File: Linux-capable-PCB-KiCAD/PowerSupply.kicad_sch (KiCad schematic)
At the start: 59 parts

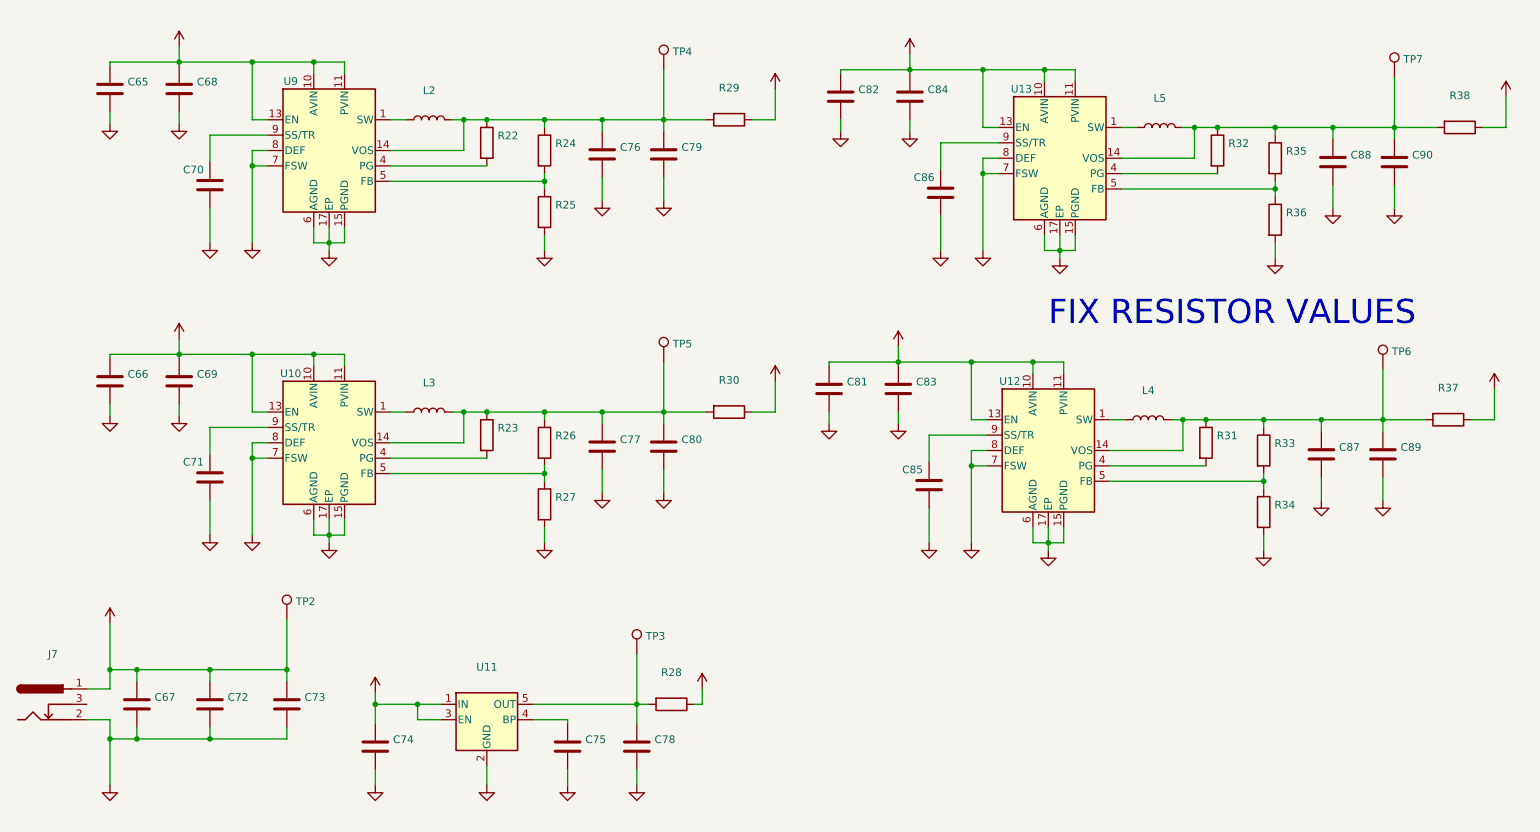
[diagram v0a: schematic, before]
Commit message: Dodao 3.3V na SD karticu, treba zamjeniti SD konektor, zavrsio napjanje, treba izracunati vrijednosti otpornika i footprint preci za komponente
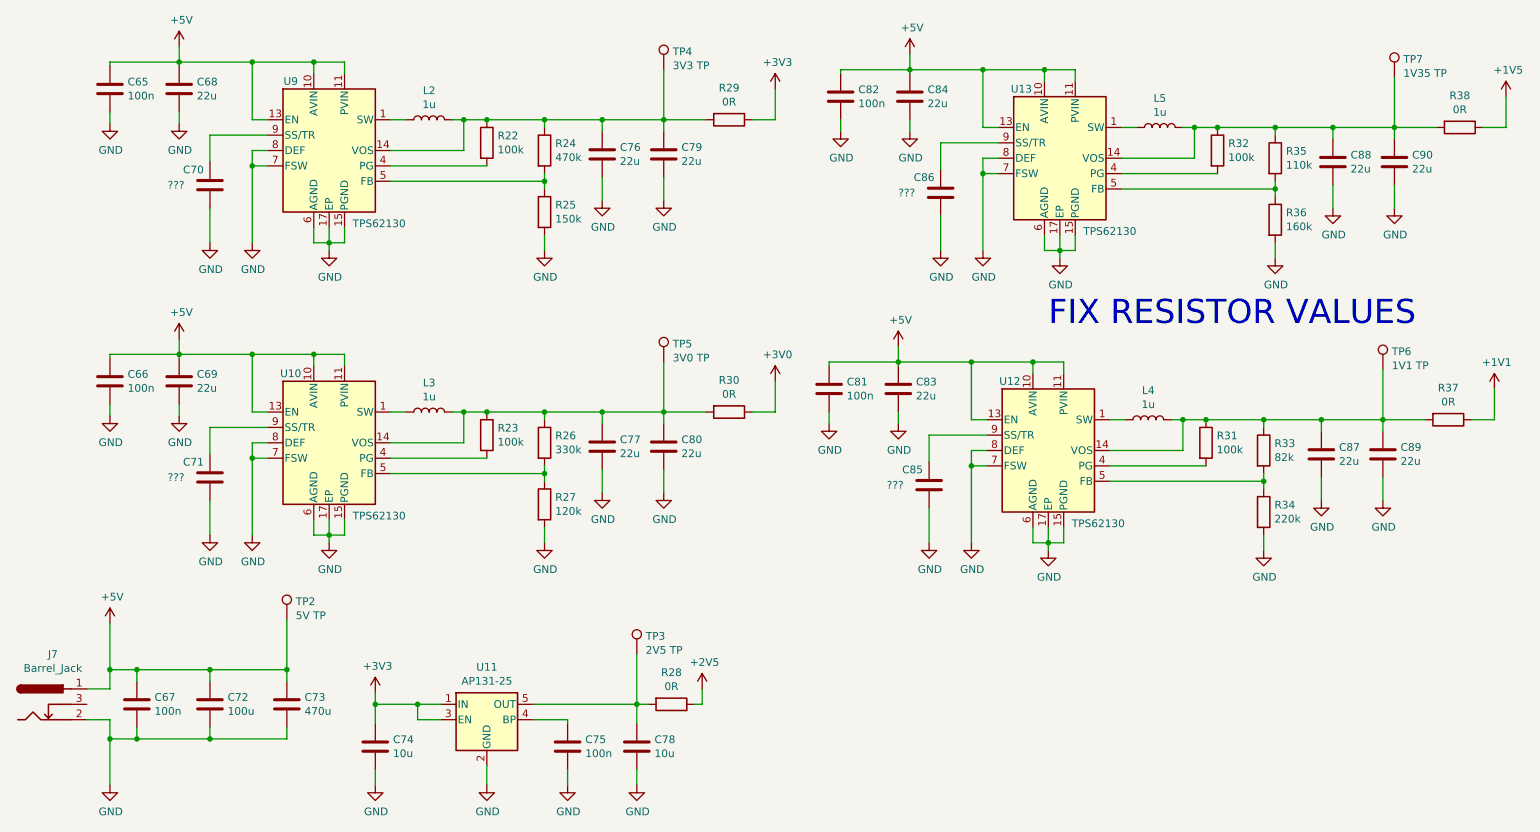
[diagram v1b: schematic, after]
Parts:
- C65, C66, C67, C75, C81, C82: value (none) -> 100n; footprint (none) -> Capacitor_SMD:C_0603_1608Metric
- C68, C69, C76, C77, C79, C80, C83, C84, C87, C88, C89, C90: value (none) -> 22u; footprint (none) -> Capacitor_SMD:C_0603_1608Metric
- C70, C71, C85, C86: value (none) -> ???; footprint (none) -> Capacitor_SMD:C_0603_1608Metric
- C72: value (none) -> 100u; footprint (none) -> Capacitor_SMD:C_0603_1608Metric
- C73: value (none) -> 470u; footprint (none) -> Capacitor_SMD:C_0603_1608Metric
- C74, C78: value (none) -> 10u; footprint (none) -> Capacitor_SMD:C_0603_1608Metric
- J7: value (none) -> Barrel_Jack; footprint (none) -> Connector_BarrelJack:BarrelJack_CUI_PJ-063AH_Horizontal
- L2, L3, L4, L5: value (none) -> 1u; footprint (none) -> Inductor_SMD:L_0603_1608Metric
- R22, R23, R31, R32: value (none) -> 100k; footprint (none) -> Resistor_SMD:R_0603_1608Metric
- R24: value (none) -> 470k; footprint (none) -> Resistor_SMD:R_0603_1608Metric
- R25: value (none) -> 150k; footprint (none) -> Resistor_SMD:R_0603_1608Metric
- R26: value (none) -> 330k; footprint (none) -> Resistor_SMD:R_0603_1608Metric
- R27: value (none) -> 120k; footprint (none) -> Resistor_SMD:R_0603_1608Metric
- R28, R29, R30, R37, R38: value (none) -> 0R; footprint (none) -> Resistor_SMD:R_0603_1608Metric
- R33: value (none) -> 82k; footprint (none) -> Resistor_SMD:R_0603_1608Metric
- R34: value (none) -> 220k; footprint (none) -> Resistor_SMD:R_0603_1608Metric
- R35: value (none) -> 110k; footprint (none) -> Resistor_SMD:R_0603_1608Metric
- R36: value (none) -> 160k; footprint (none) -> Resistor_SMD:R_0603_1608Metric
- TP2: value (none) -> 5V TP; footprint (none) -> TestPoint:TestPoint_Pad_1.0x1.0mm
- TP3: value (none) -> 2V5 TP; footprint (none) -> TestPoint:TestPoint_Pad_1.0x1.0mm
- TP4: value (none) -> 3V3 TP; footprint (none) -> TestPoint:TestPoint_Pad_1.0x1.0mm
- TP5: value (none) -> 3V0 TP; footprint (none) -> TestPoint:TestPoint_Pad_1.0x1.0mm
- TP6: value (none) -> 1V1 TP; footprint (none) -> TestPoint:TestPoint_Pad_1.0x1.0mm
- TP7: value (none) -> 1V35 TP; footprint (none) -> TestPoint:TestPoint_Pad_1.0x1.0mm
- U10, U12, U13, U9: value (none) -> TPS62130; footprint (none) -> Package_DFN_QFN:QFN-16-1EP_3x3mm_P0.5mm_EP1.7x1.7mm
- U11: value (none) -> AP131-25; footprint (none) -> Package_TO_SOT_SMD:SOT-23-5

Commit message: message
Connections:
- net +1V5 renamed +1V35
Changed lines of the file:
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@@
-    (stroke (width 0) (type default) (color 0 0 0 0))
-  )
-  (wire (pts (xy 275.59 28.575) (xy 275.59 33.655))
     (stroke (width 0) (type default) (color 0 0 0 0))
   )
@@
   )
   (wire (pts (xy 83.82 52.705) (xy 83.82 50.165))
+    (stroke (width 0) (type default) (color 0 0 0 0))
+  )
+  (wire (pts (xy 275.59 29.21) (xy 275.59 33.655))
     (stroke (width 0) (type default) (color 0 0 0 0))
   )
@@
     )
     (property "Datasheet" "" (id 3) (at 88.9 127 0)
-      (effects (font (size 1.27 1.27)) hide)
-    )
-    (pin "1")
-  )
-  (symbol (lib_id "power:+1V5") (at 275.59 28.575 0) (unit 1)
-    (in_bom yes) (on_board yes)
-    (property "Reference" "#PWR0251" (id 0) (at 275.59 32.385 0)
-      (effects (font (size 1.27 1.27)) hide)
-    )
-    (property "Value" "+1V5" (id 1) (at 275.971 24.1808 0))
-    (property "Footprint" "" (id 2) (at 275.59 28.575 0)
-      (effects (font (size 1.27 1.27)) hide)
-    )
-    (property "Datasheet" "" (id 3) (at 275.59 28.575 0)
       (effects (font (size 1.27 1.27)) hide)
     )
@@
       (effects (font (size 1.27 1.27)) hide)
     )
+    (pin "1")
+  )
+  (symbol (lib_id "power:+1V35") (at 275.59 29.21 0) (unit 1)
+    (in_bom yes) (on_board yes) (fields_autoplaced)
+    (property "Reference" "#PWR?" (id 0) (at 275.59 33.02 0)
+      (effects (font (size 1.27 1.27)) hide)
+    )
+    (property "Value" "+1V35" (id 1) (at 275.59 24.13 0))
+    (property "Footprint" "" (id 2) (at 275.59 29.21 0)
+      (effects (font (size 1.27 1.27)) hide)
+    )
+    (property "Datasheet" "" (id 3) (at 275.59 29.21 0)
+      (effects (font (size 1.27 1.27)) hide)
+    )
